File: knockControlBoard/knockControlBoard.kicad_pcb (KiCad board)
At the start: 2 copper layers, 45.2 x 51.4 mm, 43 parts, among them J1 +knock input-, J4 +12v in-, J5 +5v in-, J7 Conn_01x04, SW1 knock test, SW2 sync test, U1 NCS2250, U2 ADG601, U3 INA333xxDGK, U4 MIC920, U6 NCS2250, U7 MIC920

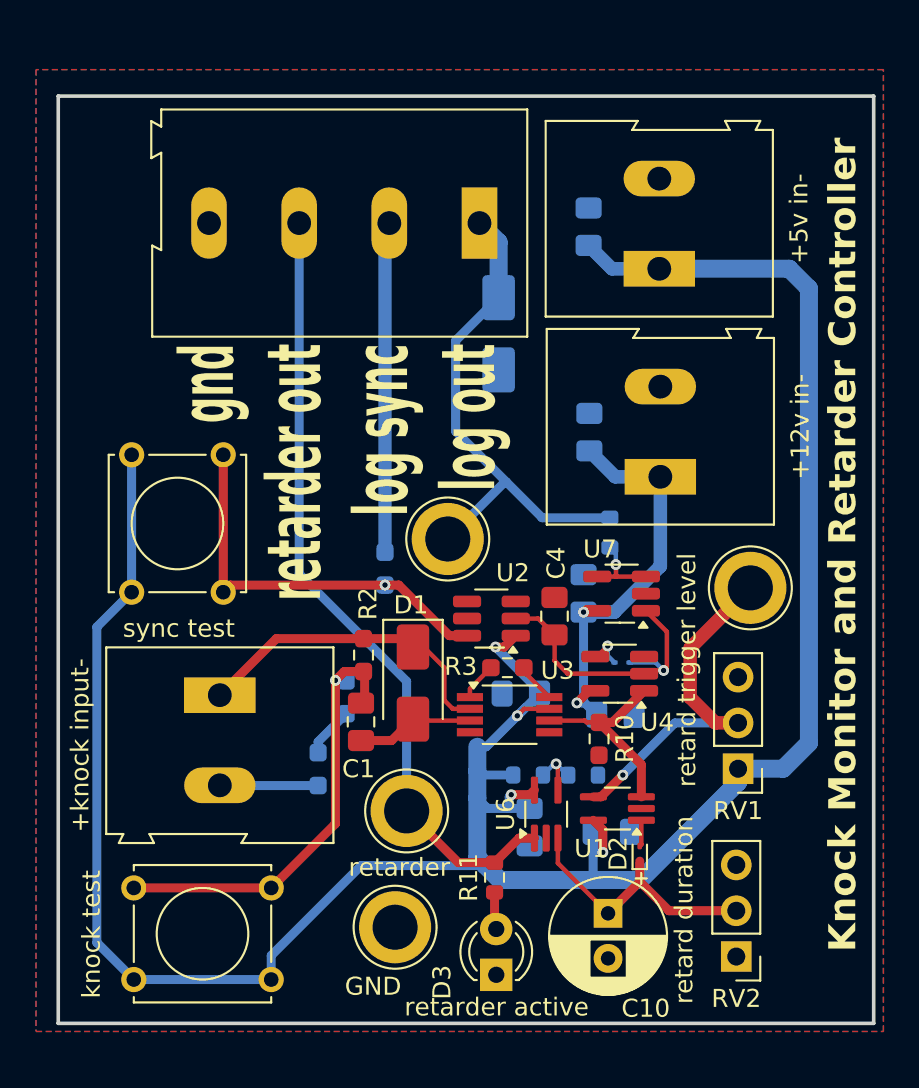
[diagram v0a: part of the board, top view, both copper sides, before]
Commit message: update
better retarder strategy
replaced mic with true rail to rail and single supply
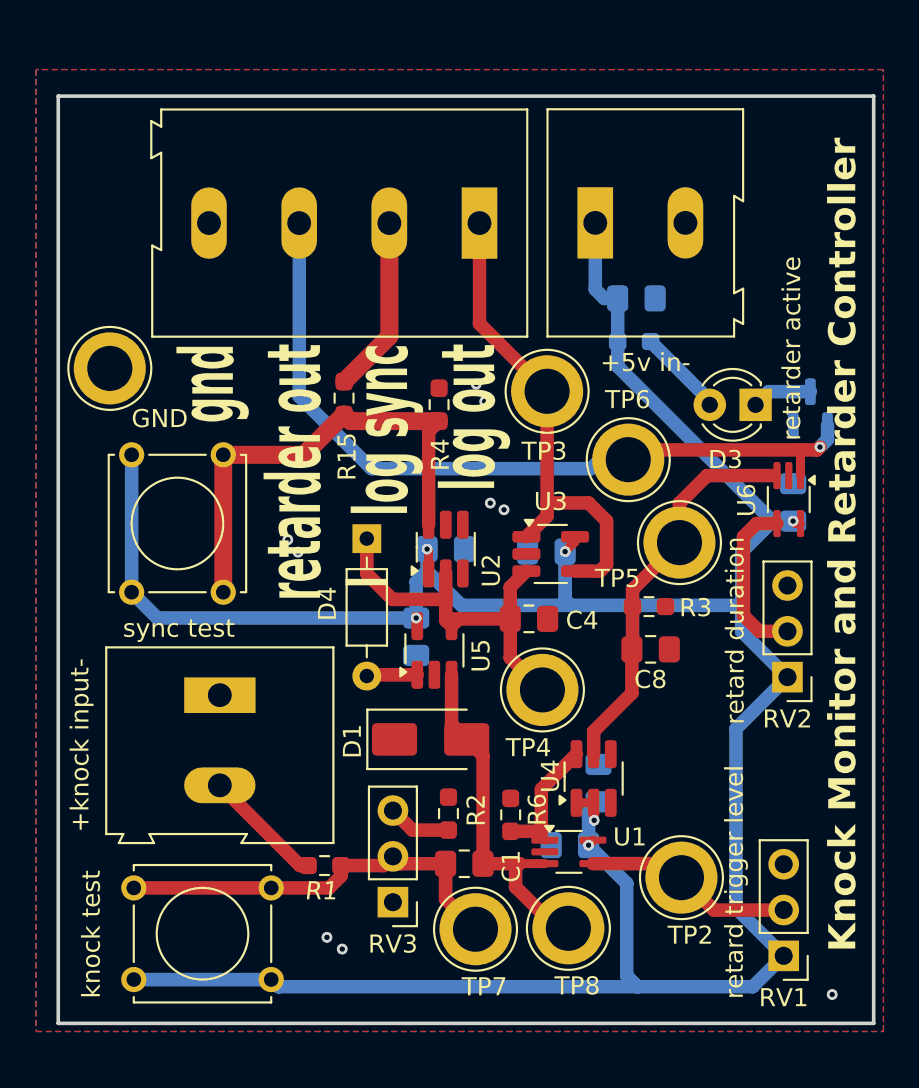
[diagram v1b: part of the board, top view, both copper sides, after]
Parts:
- removed C10: 100uF, Capacitor_THT:CP_Radial_D6.3mm_P2.50mm
- removed C12: 100nF, Capacitor_SMD:C_0805_2012Metric_Pad1.18x1.45mm_HandSolder
- removed D2, D6: CMAD6001, Diode_SMD:D_SOD-923
- removed D7: SMAJ5.0CA, Diode_SMD:D_SMA
- removed J4: +12v in-, TerminalBlock:TerminalBlock_Altech_AK300-2_P5.00mm
- removed R10: 10k, Resistor_SMD:R_0603_1608Metric_Pad0.98x0.95mm_HandSolder
- removed R12: 100k, Resistor_SMD:R_0603_1608Metric
- removed R14: 1k, Resistor_SMD:R_0603_1608Metric
- removed R5: 400k, Resistor_SMD:R_0603_1608Metric
- removed U7: MIC920, Package_TO_SOT_SMD:SOT-23-5_HandSoldering
- added C7: 100nF, Capacitor_SMD:C_0805_2012Metric_Pad1.18x1.45mm_HandSolder, B.Cu at (110.8, 90.2)
- added C8: 1uF, Capacitor_SMD:C_0805_2012Metric_Pad1.18x1.45mm_HandSolder, F.Cu at (116.6, 95.7)
- added D4: 1N4148, Diode_THT:D_DO-35_SOD27_P7.62mm_Horizontal, F.Cu at (100.9, 89.5)
- added Q1: AO3400A, Package_TO_SOT_SMD:SOT-23, B.Cu at (125.5, 82.3)
- added R6: 10k, Resistor_SMD:R_0603_1608Metric_Pad0.98x0.95mm_HandSolder, F.Cu at (108.9, 104.8)
- added RV3: input divider, Connector_PinHeader_2.54mm:PinHeader_1x03_P2.54mm_Vertical, F.Cu at (102.3, 109.7)
- added TP5: ~, TestPoint:TestPoint_Loop_D3.80mm_Drill2.5mm, F.Cu at (118.2, 89.7)
- added TP6: ~, TestPoint:TestPoint_Loop_D3.80mm_Drill2.5mm, F.Cu at (115.4, 85.1)
- added TP7: ~, TestPoint:TestPoint_Loop_D3.80mm_Drill2.5mm, F.Cu at (106.9, 111.2)
- added TP8: ~, TestPoint:TestPoint_Loop_D3.80mm_Drill2.5mm, F.Cu at (112.1, 111.1)
- added U5: AD8628, Package_TO_SOT_SMD:SOT-23-5_HandSoldering, F.Cu at (104.6, 95.7)
- C6: value 10uF -> 100nF
- R1, R15: moved to F.Cu
- R11: footprint Resistor_SMD:R_0603_1608Metric -> Resistor_SMD:R_0603_1608Metric_Pad0.98x0.95mm_HandSolder; moved to B.Cu
- R2: value 150k -> 100k
- R3: value 100k -> 10M
- R4: value 150k -> 10k; moved to F.Cu
- TP4: value retarder -> ~
- U3: value INA333xxDGK -> AD8628; footprint Package_SO:VSSOP-8_3.0x3.0mm_P0.65mm -> Package_TO_SOT_SMD:SOT-23-5_HandSoldering
- U4: value MIC920 -> ADG601; footprint Package_TO_SOT_SMD:SOT-23-5_HandSoldering -> Package_TO_SOT_SMD:SOT-23-6_Handsoldering
- moved TP1 34.8 mm to (86.6, 80.1)
- moved D3 34.7 mm to (122.5, 82.1), turned to 180 degrees
- moved R11 30.7 mm to (115.7, 78.6), turned to 180 degrees
- moved C11 23.2 mm to (124.5, 87.5), turned to -90 degrees
- moved U6 22.0 mm to (124.3, 87.3), turned to -90 degrees
- moved C6 19.5 mm to (113.7, 103.1), turned to -90 degrees
- moved R4 17.0 mm to (104.9, 82.1), turned to -90 degrees
- moved TP2 16.5 mm to (118.3, 108.3), turned to 0 degrees
- moved RV2 15.8 mm to (124.2, 97.2)
- moved C3 13.2 mm to (105.3, 90.1)
- moved RV1 10.7 mm to (124.0, 112.6)
- moved TP4 10.1 mm to (110.6, 97.9)
- moved R2 9.97 mm to (105.4, 104.8)
- moved TP3 9.87 mm to (110.9, 81.3), turned to 90 degrees
- moved C1 9.73 mm to (106.3, 107.5), turned to 0 degrees
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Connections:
- C3 pad 2: +12V -> +5V
- C4 pad 2: Net-(D6-K) -> Net-(D4-K)
- C6 pad 1: +12V -> GND
- C6 pad 2: GND -> +5V
- D1 pad 1: Net-(D1-A1) -> GND
- D3 pad 1: GND -> Net-(D3-K)
- J1 pad 1: Net-(D1-A1) -> GND
- R1 pad 2: Net-(R1-Pad2) -> Net-(C1-Pad1)
- R11 pad 2: retarder_out -> +5V
- R2 pad 1: Net-(C1-Pad1) -> Net-(R2-Pad1)
- R2 pad 2: Net-(D1-A1) -> GND
- R3 pad 1: Net-(R3-Pad1) -> GND
- R3 pad 2: Net-(R3-Pad2) -> Net-(U4-D)
- R4 pad 1: Net-(R1-Pad2) -> GND
- R4 pad 2: Net-(C1-Pad1) -> Net-(U2-IN)
- RV2 pad 1: unconnected-(RV2-Pad1) -> +5V
- RV2 pad 2: Net-(D2-K) -> Net-(U6-IN-)
- TP4 pad 1: retarder_out -> Net-(D4-K)
- U1 pad 1: Net-(D2-A) -> Net-(U1-OUT)
- U1 pad 3: Net-(U1-IN+) -> Net-(D1-A2)
- U2 pad 2: Net-(D6-K) -> Net-(D4-K)
- U3 pad 1: Net-(R3-Pad1) -> log_out
- U3 pad 2: Net-(D1-A1) -> GND
- U3 pad 3: Net-(D1-A2) -> Net-(D4-K)
- U3 pad 4: GND -> log_out
- U3 pad 5: GND -> +5V
- U4 pad 1: Net-(U1-IN+) -> +5V
- U4 pad 2: Net-(D6-K) -> +5V
- U4 pad 4: Net-(D6-A) -> GND
- U4 pad 5: +12V -> Net-(U4-D)
- U6 pad 3: Net-(D2-K) -> Net-(U4-D)
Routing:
- net +12V: track 23.3 -> 0.00 mm, vias 2 -> 0
- net Net-(U4-D): track 0.00 -> 21.8 mm
- net Net-(D4-K): track 0.00 -> 21.1 mm
- net Net-(D1-A1): track 17.8 -> 0.00 mm
- net Net-(D6-K): track 16.3 -> 0.00 mm, vias 1 -> 0
- net Net-(D2-K): track 15.0 -> 0.00 mm
- net Net-(D1-A2): track 6.56 -> 19.8 mm
- net Net-(U1-IN+): track 11.1 -> 0.00 mm
- net +5V: track 145.7 -> 155.1 mm, vias 4 -> 6
- net Net-(U1-IN-): track 20.4 -> 11.6 mm, vias 1 -> 0
- net log_sync: track 18.3 -> 9.83 mm
- net Net-(U1-OUT): track 0.00 -> 7.41 mm
- net Net-(U6-IN-): track 3.41 -> 9.34 mm, vias 1 -> 0
- net Net-(U7-IN-): track 4.45 -> 0.00 mm, vias 1 -> 0
- net Net-(U2-IN): track 22.5 -> 26.7 mm, vias 1 -> 0
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
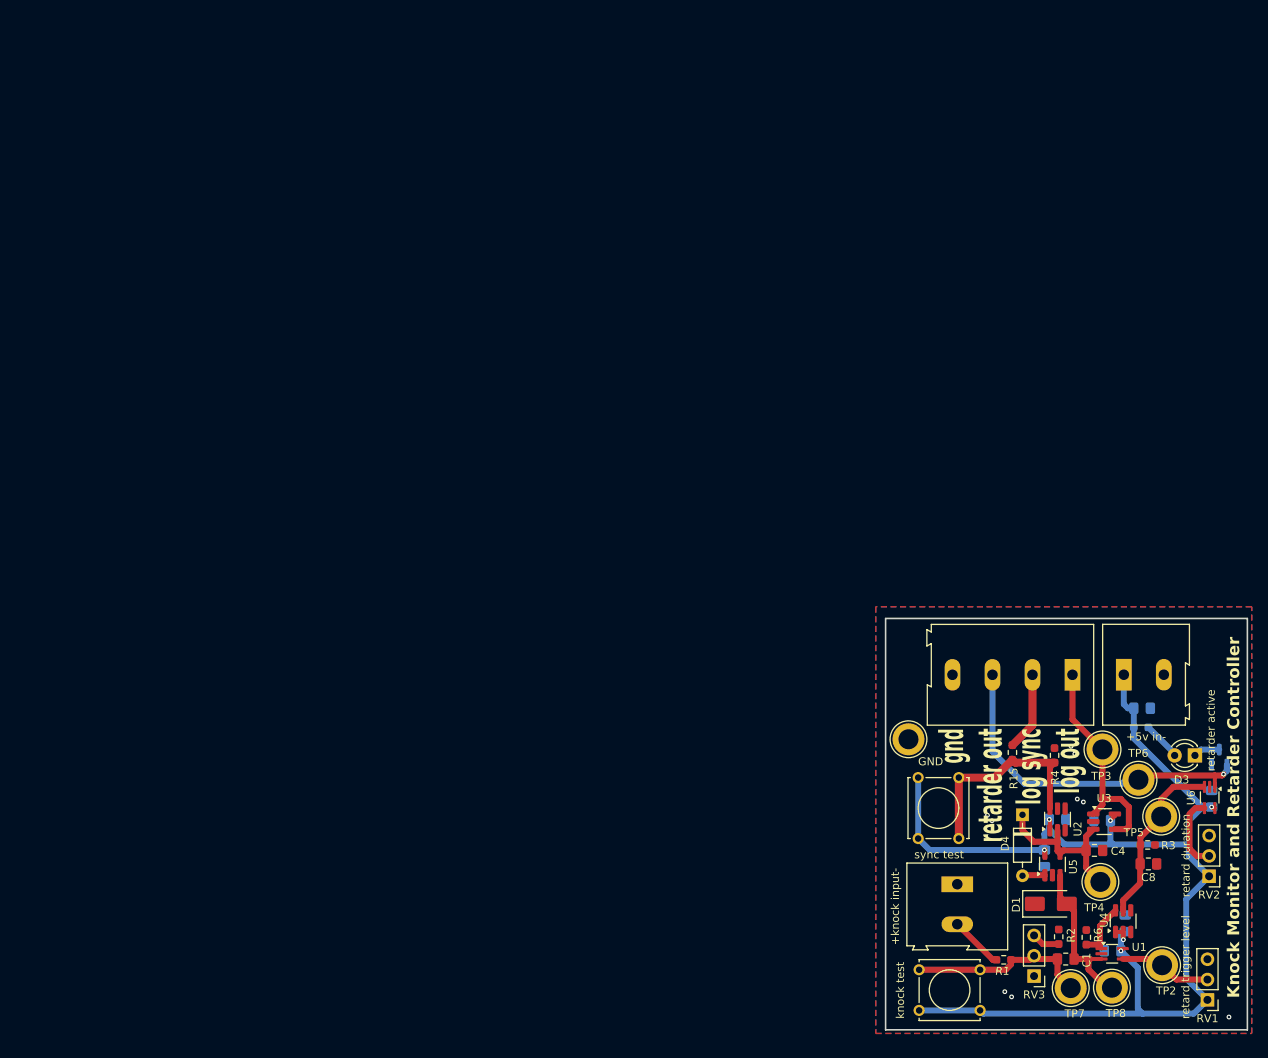
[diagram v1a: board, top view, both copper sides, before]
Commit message: WIP daisy chain, final boards
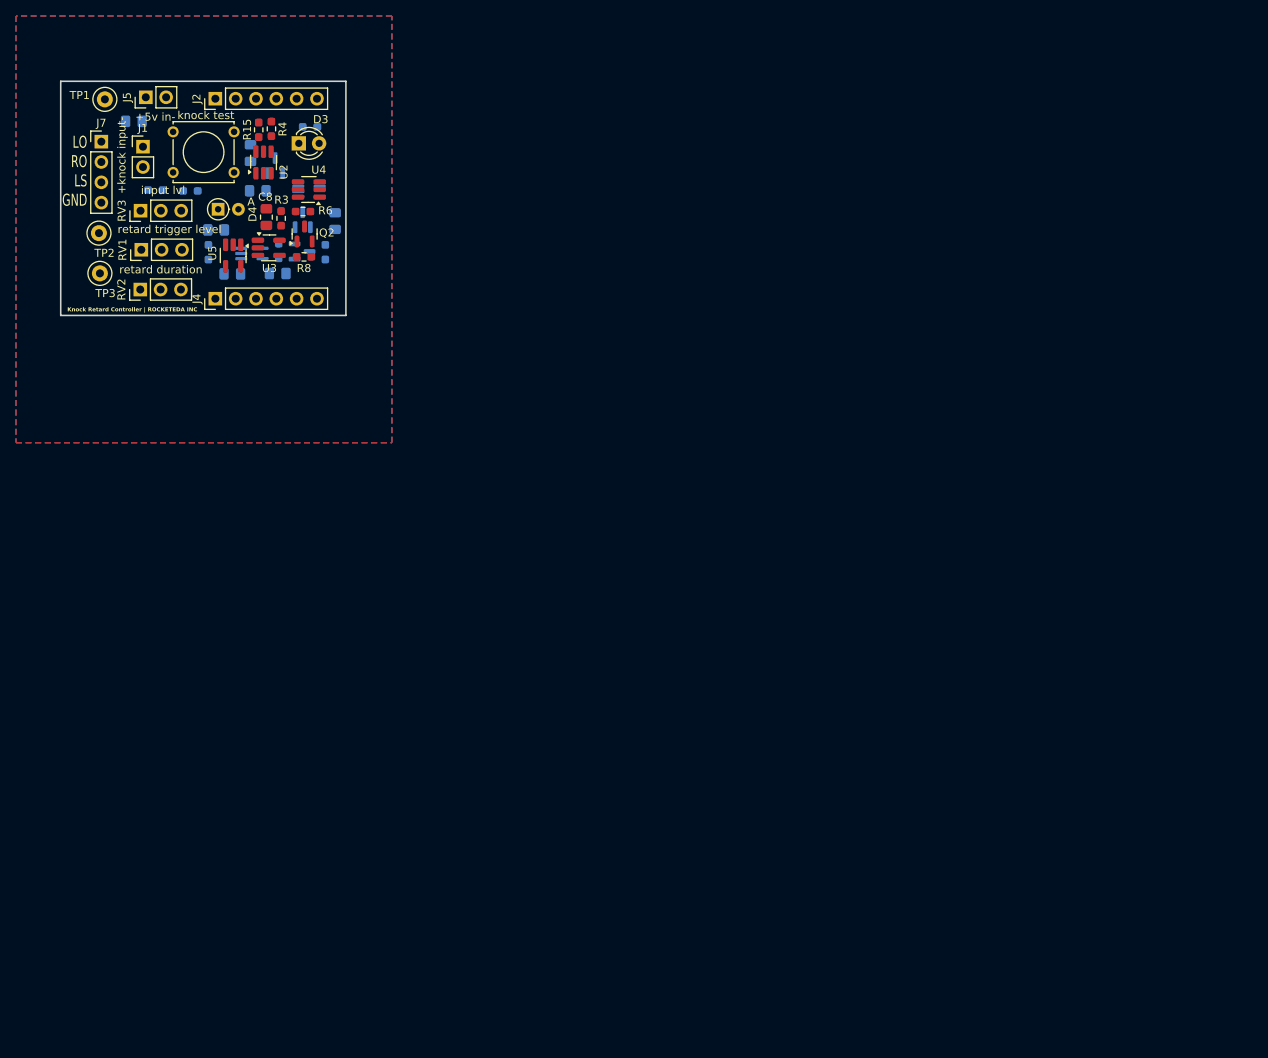
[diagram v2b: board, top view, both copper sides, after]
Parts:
- removed C2, C6: 100nF, Capacitor_SMD:C_0805_2012Metric_Pad1.18x1.45mm_HandSolder
- removed D1: SMAJ5.0CA, Diode_SMD:D_SMA
- removed SW2: sync test, Button_Switch_THT:SW_Tactile_Straight_KSA0Axx1LFTR
- removed TP4, TP5, TP6, TP7, TP8: ~, TestPoint:TestPoint_Loop_D3.80mm_Drill2.5mm
- added J2: Conn_01x06, Connector_PinHeader_2.54mm:PinHeader_1x06_P2.54mm_Vertical, F.Cu at (0.00, 0.00)
- added J4: Conn_01x06, Connector_PinHeader_2.54mm:PinHeader_1x06_P2.54mm_Vertical, F.Cu at (0.00, 25.0)
- added Q2: AO3400A, Package_TO_SOT_SMD:SOT-23, F.Cu at (11.2, 16.9)
- added Q3: AO3400A, Package_TO_SOT_SMD:SOT-23, B.Cu at (10.9, 15.1)
- added Q4: AO3400A, Package_TO_SOT_SMD:SOT-23, B.Cu at (10.8, 19.1)
- added R10: 10k, Resistor_SMD:R_0603_1608Metric_Pad0.98x0.95mm_HandSolder, B.Cu at (13.7, 19.2)
- added R5: 3M, Resistor_SMD:R_0603_1608Metric_Pad0.98x0.95mm_HandSolder, B.Cu at (-0.87, 19.2)
- added R7: 10k, Resistor_SMD:R_0603_1608Metric_Pad0.98x0.95mm_HandSolder, B.Cu at (7.92, 19.0)
- added R8: 10k, Resistor_SMD:R_0603_1608Metric_Pad0.98x0.95mm_HandSolder, F.Cu at (11.1, 19.8)
- C1, C4, R1, R2, U1, U6: moved to B.Cu
- D4: footprint Diode_THT:D_DO-35_SOD27_P7.62mm_Horizontal -> Diode_THT:D_DO-35_SOD27_P2.54mm_Vertical_AnodeUp
- J1, J5: footprint TerminalBlock:TerminalBlock_Altech_AK300-2_P5.00mm -> Connector_PinHeader_2.54mm:PinHeader_1x02_P2.54mm_Vertical
- J7: footprint TerminalBlock:TerminalBlock_Altech_AK300-4_P5.00mm -> Connector_PinHeader_2.54mm:PinHeader_1x04_P2.54mm_Vertical
- RV3: value input divider -> input lvl
- TP1, TP2: footprint TestPoint:TestPoint_Loop_D3.80mm_Drill2.5mm -> TestPoint:TestPoint_Loop_D1.80mm_Drill1.0mm_Beaded
- TP3: value datalogger output -> ~; footprint TestPoint:TestPoint_Loop_D3.80mm_Drill2.5mm -> TestPoint:TestPoint_Loop_D1.80mm_Drill1.0mm_Beaded
- moved RV1 162.9 mm to (-9.26, 18.9), turned to 90 degrees
- moved TP2 161.4 mm to (-14.6, 16.8)
- moved RV2 152.4 mm to (-9.38, 23.9), turned to 90 degrees
- moved SW1 149.1 mm to (-5.28, 4.14), turned to 0 degrees
- moved RV3 147.1 mm to (-9.35, 14.0), turned to 90 degrees
- moved C9 145.8 mm to (-10.2, 2.83), turned to 180 degrees
- moved R1 143.2 mm to (-7.50, 11.4)
- moved R2 143.1 mm to (-3.12, 11.5), turned to 0 degrees
- moved J5 142.0 mm to (-8.70, -0.18), turned to 90 degrees
- moved C1 139.9 mm to (0.10, 16.4)
- moved Q1 139.3 mm to (7.47, 8.36)
- moved C5 138.8 mm to (2.12, 21.9)
- moved TP3 138.7 mm to (-14.4, 21.8), turned to 0 degrees
- moved U1 138.7 mm to (4.57, 19.3)
- moved J7 138.5 mm to (-14.2, 5.37), turned to 0 degrees
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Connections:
- net Net-(U1-IN-) renamed retard_trig_lvl
- J7 pad 2: log_sync -> retarder_out
- J7 pad 3: retarder_out -> log_sync
- R6 pad 1: GND -> Net-(Q3-D)
- R6 pad 2: Net-(U1-OUT) -> +5V
- RV2 pad 2: Net-(U6-IN-) -> retard duration
- TP3 pad 1: log_out -> retard duration
- U1 pad 1: Net-(U1-OUT) -> Net-(Q4-G)
- U4 pad 6: Net-(U1-OUT) -> Net-(Q3-D)
- U6 pad 4: Net-(U6-IN-) -> retard duration
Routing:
- net +5V: track 155.1 -> 0.00 mm, vias 6 -> 0
- net retarder_out: track 43.4 -> 0.00 mm, vias 1 -> 0
- net log_out: track 27.5 -> 0.00 mm
- net Net-(U2-IN): track 26.7 -> 0.00 mm
- net Net-(C1-Pad1): track 22.8 -> 0.00 mm
- net Net-(U4-D): track 21.8 -> 0.00 mm
- net Net-(D4-K): track 21.1 -> 0.00 mm
- net Net-(U1-IN+): track 19.8 -> 0.00 mm
- net retard_trig_lvl: track 11.6 -> 0.00 mm
- net log_sync: track 9.83 -> 0.00 mm
- net Net-(U6-IN-): track 9.34 -> 0.00 mm
- net Net-(U1-OUT): track 7.41 -> 0.00 mm
- net Net-(J1-Pin_2): track 6.74 -> 0.00 mm
- net Net-(D3-A): track 4.87 -> 0.00 mm
- net Net-(R2-Pad1): track 3.53 -> 0.00 mm
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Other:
- board size 45.2 x 51.4 mm -> 35.6 x 29.3 mm
- board text added: "Knock Retard Controller | ROCKETEDA INC"
- board text added: "LO RO LS GND"
- board text removed: "Knock Monitor and Retarder Controller"
- board text removed: "gnd retarder out log sync log out"

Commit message: hopefully final
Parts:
- moved Q1 2.30 mm to (7.43, 6.06)
- moved C4 1.07 mm to (5.83, 12.4)
- moved C11 1.05 mm to (13.9, 15.3)
- moved U1 0.69 mm to (4.56, 18.6)
- moved R7 0.52 mm to (8.09, 19.5)
- moved R8 0.50 mm to (11.6, 19.8)
- moved C7 0.40 mm to (7.74, 22.2)
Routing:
- net +5V: track 0.00 -> 105.8 mm, vias 0 -> 6
- net log_sync: track 0.00 -> 68.4 mm
- net retard_trig_lvl: track 0.00 -> 63.9 mm, vias 0 -> 1
- net retard duration: track 0.00 -> 62.5 mm
- net log_out: track 0.00 -> 32.4 mm, vias 0 -> 2
- net retarder_out: track 0.00 -> 32.3 mm, vias 0 -> 2
- net retarder_trig: track 0.00 -> 30.3 mm, vias 0 -> 2
- net Net-(D4-K): track 0.00 -> 22.0 mm, vias 0 -> 2
- net Net-(C1-Pad1): track 0.00 -> 19.9 mm
- net retarder_in: track 0.00 -> 8.73 mm, vias 0 -> 1
- net Net-(Q4-G): track 0.00 -> 8.39 mm
- net Net-(U4-D): track 0.00 -> 7.85 mm, vias 0 -> 1
- net Net-(U1-IN+): track 0.00 -> 6.83 mm, vias 0 -> 1
- net Net-(D4-A): track 0.00 -> 4.55 mm
- net Net-(U2-IN): track 0.00 -> 3.60 mm
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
